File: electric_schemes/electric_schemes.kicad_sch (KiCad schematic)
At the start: 8 parts, among them M1 Motor_DC, M2 Motor_DC, M3 Motor_Servo, M4 Motor_Servo, U1 RaspberryPi-CM1, U2 L298N, U3 LM3478MA

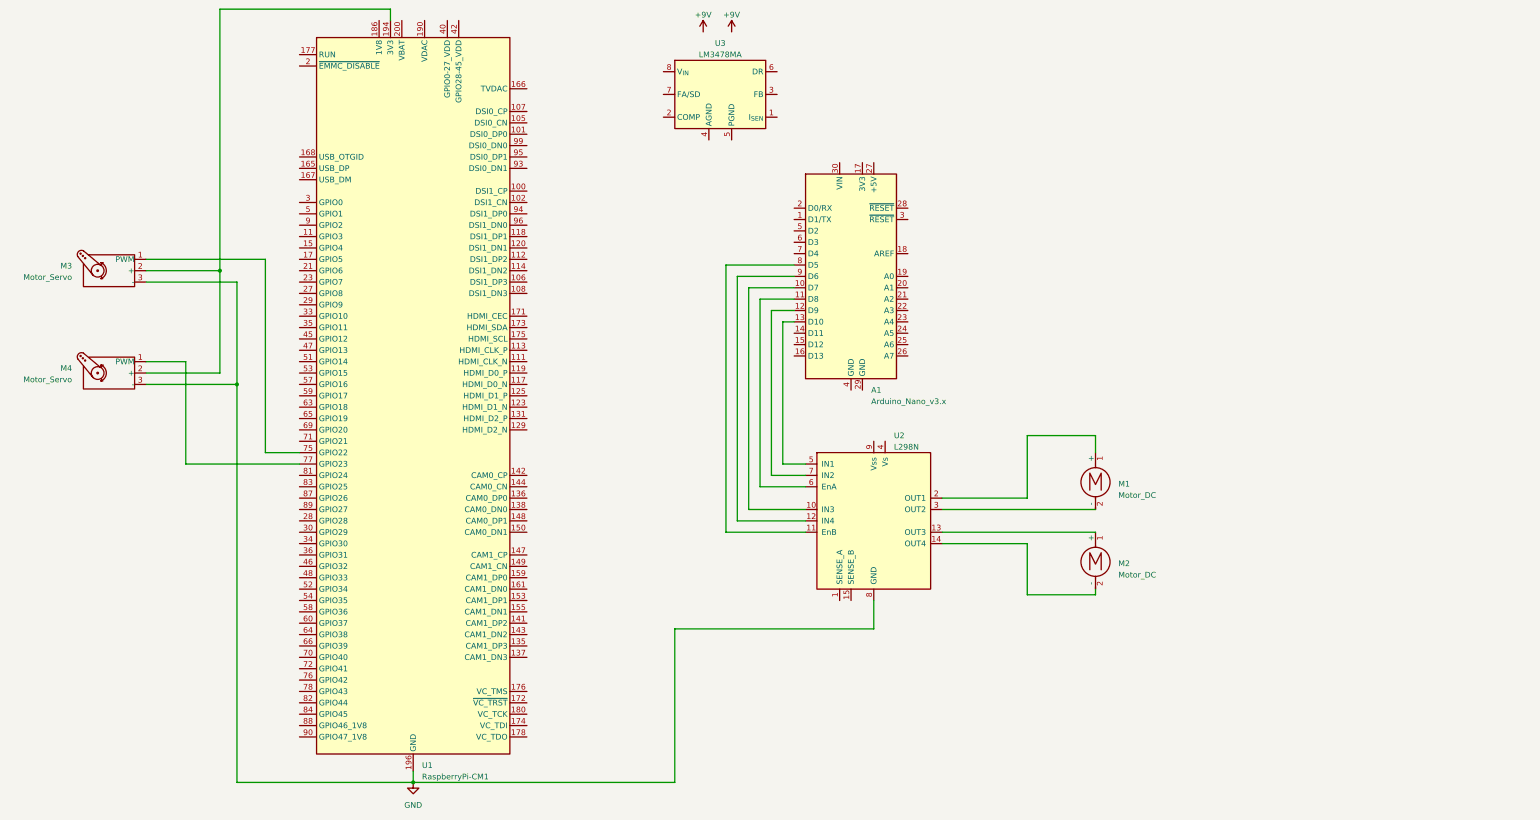
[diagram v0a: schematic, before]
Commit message: update electric schemes, test from control dc motors arduino
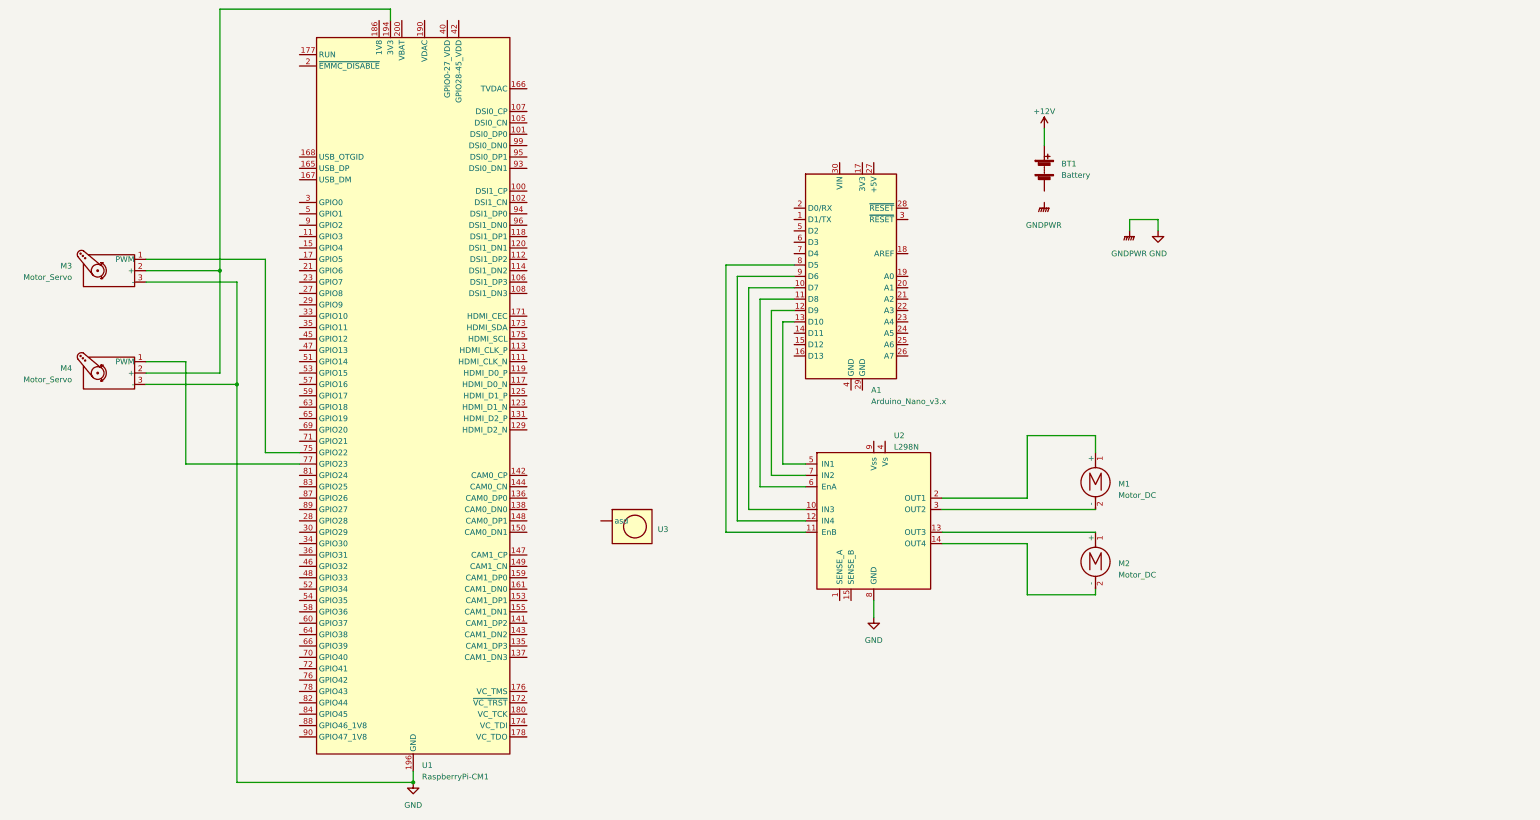
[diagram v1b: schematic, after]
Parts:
- removed U3: LM3478MA, Package_SO:SOIC-8_3.9x4.9mm_P1.27mm, symbol Regulator_Controller:LM3478MA
- added BT1: Battery, symbol Device:Battery
- added U3: ~, symbol project_library:RPI_camera_v2
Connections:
- new net +12V: BT1.1 (+)
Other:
- title: (none) -> Schemes electric Scorpion balance board

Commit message: upgrade schemes electric
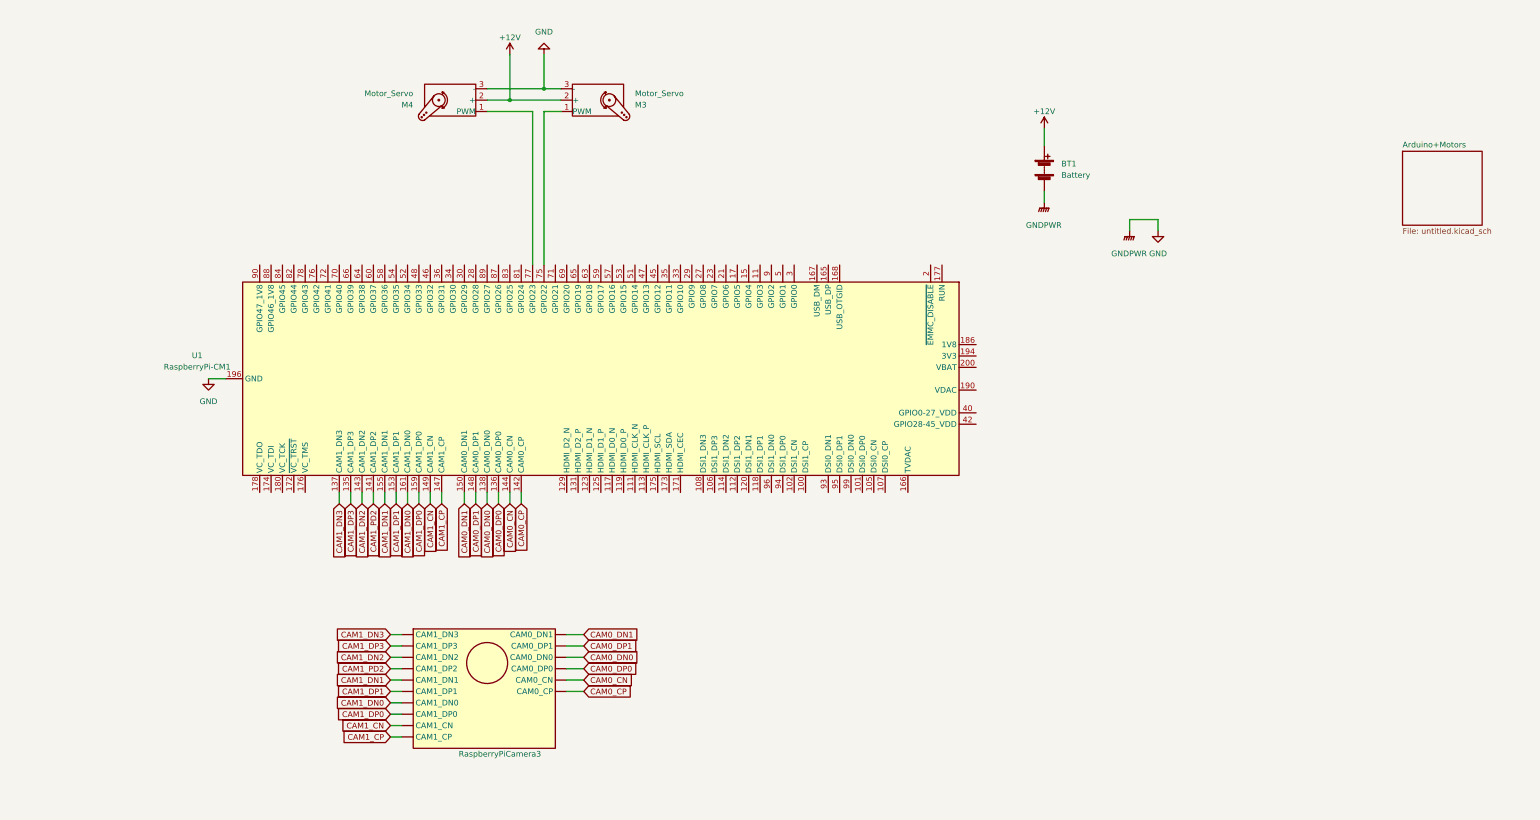
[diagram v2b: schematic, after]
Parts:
- removed A1: Arduino_Nano_v3.x, Module:Arduino_Nano, symbol MCU_Module:Arduino_Nano_v3.x
- removed M1, M2: Motor_DC, symbol Motor:Motor_DC
- removed U2: L298N, Package_TO_SOT_THT:TO-220-15_P2.54x2.54mm_StaggerOdd_Lead4.58mm_Vertical, symbol Driver_Motor:L298N
- renumbered U3 to RaspberryPiCamera3
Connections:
- net +12V: now also M3.2 (+), M4.2 (+)
- net GND: now also BT1.2 (-)
- net CAM1_PD2: now reaches RaspberryPiCamera3. (CAM1_DP3)
- net CAM1_PD2: now also U1.141 (CAM1_DP2)
- net at U1.191 (3V3), U1.192 (3V3), U1.193 (3V3)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: no longer M3.2 (+), M4.2 (+)
- net CAM1_DP3: now reaches U1.135 (CAM1_DP3)
- net CAM1_DP3: now also RaspberryPiCamera3. (CAM1_DP3)
- net CAM0_DP0: now reaches U1.136 (CAM0_DP0)
- net CAM0_DP0: now also RaspberryPiCamera3. (CAM1_DP3)
- net CAM1_DN3: now reaches U1.137 (CAM1_DN3)
- net CAM1_DN3: now also RaspberryPiCamera3. (CAM1_DP3)
- net CAM0_DN0: now reaches U1.138 (CAM0_DN0)
- net CAM0_DN0: now also RaspberryPiCamera3. (CAM1_DP3)
- net CAM0_CP: now reaches U1.142 (CAM0_CP)
- net CAM0_CP: now also RaspberryPiCamera3. (CAM1_DP3)
- net CAM1_DN2: now reaches U1.143 (CAM1_DN2)
- net CAM1_DN2: now also RaspberryPiCamera3. (CAM1_DP3)
- net CAM0_CN: now reaches U1.144 (CAM0_CN)
- net CAM0_CN: now also RaspberryPiCamera3. (CAM1_DP3)
- net CAM1_CP: now reaches U1.147 (CAM1_CP)
- net CAM1_CP: now also RaspberryPiCamera3. (CAM1_DP3)
- net CAM0_DP1: now reaches U1.148 (CAM0_DP1)
- net CAM0_DP1: now also RaspberryPiCamera3. (CAM1_DP3)
- net CAM1_CN: now reaches U1.149 (CAM1_CN)
- net CAM1_CN: now also RaspberryPiCamera3. (CAM1_DP3)
- net CAM0_DN1: now reaches U1.150 (CAM0_DN1)
- net CAM0_DN1: now also RaspberryPiCamera3. (CAM1_DP3)
- net CAM1_DP1: now reaches U1.153 (CAM1_DP1)
- net CAM1_DP1: now also RaspberryPiCamera3. (CAM1_DP3)
- net CAM1_DN1: now reaches U1.155 (CAM1_DN1)
- net CAM1_DN1: now also RaspberryPiCamera3. (CAM1_DP3)
- net CAM1_DP0: now reaches U1.159 (CAM1_DP0)
- net CAM1_DP0: now also RaspberryPiCamera3. (CAM1_DP3)
- net CAM1_DN0: now reaches U1.161 (CAM1_DN0)
- net CAM1_DN0: now also RaspberryPiCamera3. (CAM1_DP3)
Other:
- added sheet Arduino+Motors (untitled.kicad_sch)
- moved on the sheet: M3, M4, U1

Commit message: software
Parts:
- added U3, U4: APE1707M-12-HF, Package_SO:SOIC-8_3.9x4.9mm_P1.27mm, symbol Regulator_Switching:APE1707M-12-HF
- renumbered M4 to AxisX, M3 to AxisY
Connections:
- net +12V: now also U1.197 (VBAT), U1.198 (VBAT), U1.199 (VBAT), U1.200 (VBAT), U3.4 (~{EN}), U3.5 (VSS), U3.6 (VSS), U3.7 (VSS), U3.8 (VSS), U4.4 (~{EN}), U4.5 (VSS), U4.6 (VSS), U4.7 (VSS), U4.8 (VSS)
- net GND: now also U4.3 (FB); no longer BT1.2 (-)
- new net: BT1.2 (-), U3.1 (VCC), U4.1 (VCC)
- new net GNDPWR: U3.2 (SW), U3.3 (FB), U4.2 (SW)
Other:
- moved on the sheet: BT1
